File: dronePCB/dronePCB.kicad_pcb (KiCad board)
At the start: 6 copper layers, 60.4 x 98.2 mm, 207 parts, among them IC1 STUSB4500QTR, IC2 MP2338GTL-Z, IC3 DPS368XTSA1, IC4 ICM-42688-P, J1 BM03B-SRSS-TB, J10 DVR, J11 Strobe top, J12 Strobe bottom, J13 ToF400C, J14 ToF400C, J15 ToF400C, J16 ToF400C, J17 ToF400C, J18 DSHOT, J19 ESC_POW, J2 USB_C_Receptacle, J3 103AT-2 10k, J4 XT30, J5 JST, J6 Camera, J7 VID_ANT, J8 GEP-M10Q, J9 Avatar GMx, Q1 BSS138, Q2 BSS138, Q3 SQD40031EL_GE3, Q4 2N7002A, SW1 SW_BOOT, SW2 SW_RESET, SW3 SW_CHG_RST, SW4 CJS-1200TB1, SW5 CJS-1200TB1, SW6 CJS-1200TB1, SW7 SW_Push, U1 RP2350_80QFN, U10 TF-01A, U2 W25Q128JVPIQ, U3 APS6404L-3SQR-ZR, U4 BQ25792RQMR, U5 NCP1117-3.3_SOT223, U6 BQ76920PW, U7 E28-2G4M12SX, U8 AT7456E, U9 TX5823, X1 OT2EL4C4JI-111OLP-27M, Y1 ABM8-272-T3

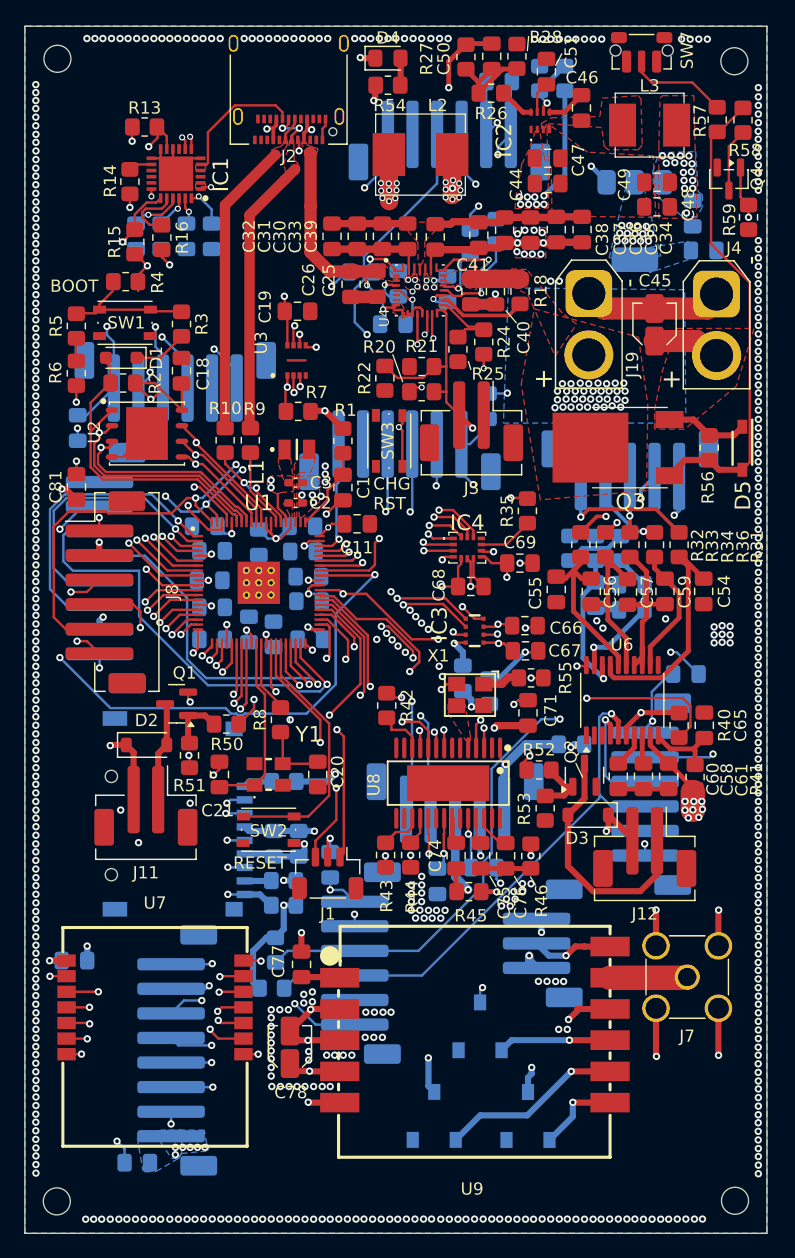
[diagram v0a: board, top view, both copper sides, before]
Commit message: Started filling the BoM and changed some components
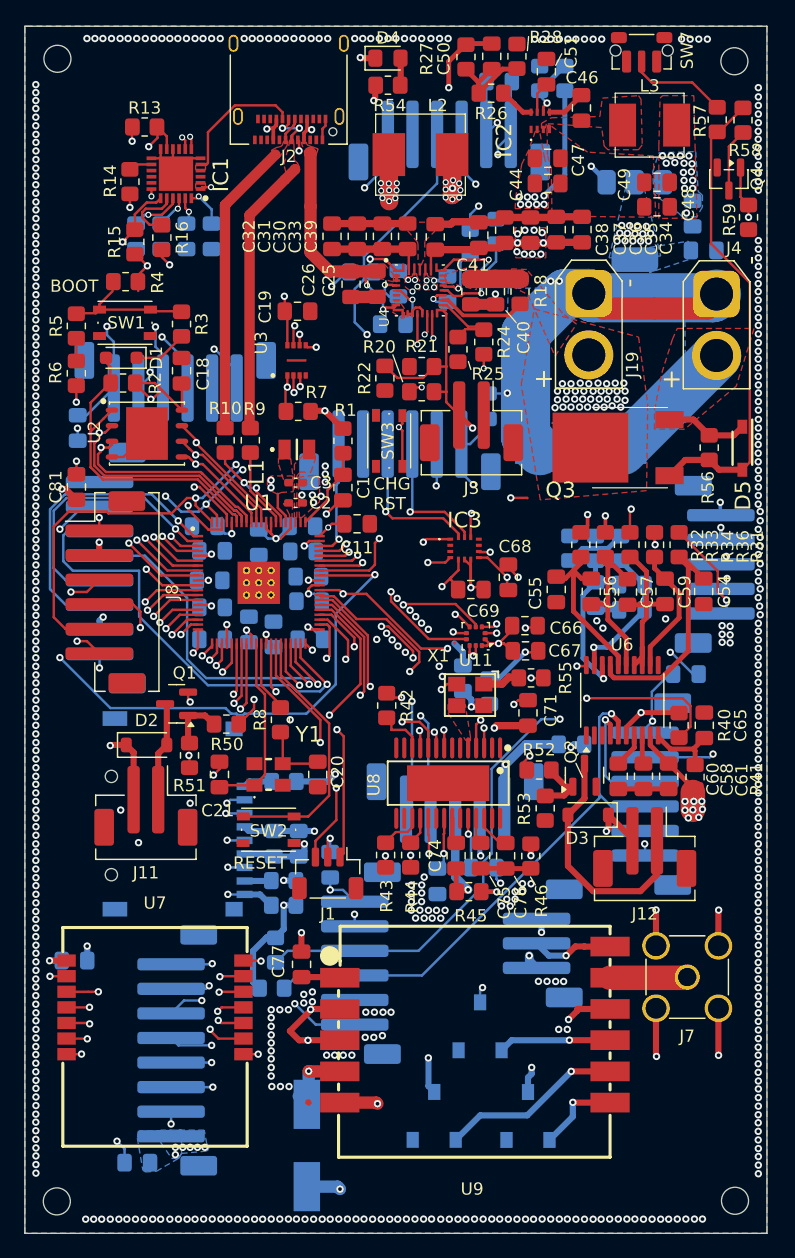
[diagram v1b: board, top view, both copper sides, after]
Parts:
- removed IC4: ICM-42688-P, droneParts:IIM42352
- removed R35: 10k, Resistor_SMD:R_0805_2012Metric_Pad1.20x1.40mm_HandSolder
- added U11: LPS22HH, Package_LGA:ST_HLGA-10_2x2mm_P0.5mm_LayoutBorder3x2y, F.Cu at (156.3, 101.3)
- C45, C78: footprint Capacitor_SMD:C_Elec_3x5.4 -> droneParts:CAPAE830X1080N; moved to B.Cu
- C89: value 0.1uf -> 100n
- C90: value 10uF -> 10u
- D1: value NSR0530HT1G -> ARB551V-30-HF
- D4: value LED -> BLUE
- IC3: value DPS368XTSA1 -> BMI323; footprint droneParts:DPS368XTSA1 -> droneParts:BMI323
- J19: value ESC_POW -> XT30
- moved C45 11.9 mm to (164.9, 86.2), turned to 180 degrees
- moved J5 10.3 mm to (175.8, 95.5), turned to -90 degrees
- moved C78 8.11 mm to (142.6, 142.8), turned to -90 degrees
- moved IC3 6.75 mm to (155.4, 94.2), turned to 0 degrees
- moved C69 4.53 mm to (155.9, 97.5)
- moved C68 3.14 mm to (159.0, 96.5), turned to 90 degrees
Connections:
- IC3 pad 2: /DPS_CS -> unconnected-(IC3-NC_1-Pad2)
- IC3 pad 3: /SPI_TX -> unconnected-(IC3-NC_2-Pad3)
- IC3 pad 4: /SPI_SCK -> /BMI_INT1
- IC3 pad 5: /SPI_RX -> +3V3
- IC3 pad 6: +3V3 -> GND
- U1 pad 23: /ICM_INT1 -> /BMI_INT1
- U1 pad 25: /ICM_INT2 -> /BMI_INT2
- U1 pad 26: /IMU_CS -> /LPSINT
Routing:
- net /IMU_CS: track 33.2 -> 0.00 mm, vias 3 -> 0
- net /ICM_INT2: track 29.8 -> 0.00 mm, vias 4 -> 0
- net /BMI_INT2: track 0.00 -> 29.5 mm, vias 0 -> 4
- net /LPSINT: track 0.00 -> 28.7 mm, vias 0 -> 2
- net /BMI_INT1: track 0.00 -> 26.7 mm, vias 0 -> 4
- net /ICM_INT1: track 26.5 -> 0.00 mm, vias 4 -> 0
- net GND: track 199.7 -> 225.0 mm, vias 523 -> 513
- net /SPI_RX: track 103.4 -> 93.3 mm, vias 8 -> 7
- net /SPI_TX: track 112.7 -> 103.2 mm, vias 10 -> 9
- net /RP2350B/Power Circuit/CELL3: track 4.56 -> 13.7 mm, vias 1 -> 2
- net /SPI_SCK: track 106.3 -> 98.5 mm
- net /I2C_SCL: track 207.2 -> 214.2 mm
- net /I2C_SDA: track 215.3 -> 220.8 mm
- net /RP2350B/Power Circuit/CELL2: track 6.97 -> 12.3 mm
- net /RP2350B/Power Circuit/BATS: track 12.5 -> 17.7 mm
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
